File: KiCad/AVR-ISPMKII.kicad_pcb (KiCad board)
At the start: 2 copper layers, 30 x 17.8 mm, 32 parts, among them J1 USB_C_Receptacle_USB2.0, J2 Self_Program, J3 V_Target, J4 ISP_Header, U1 ATmega16U2-MU, U2 AP7365-33WG-7, U3 NLSX4373DMR2G, Y1 16MHz

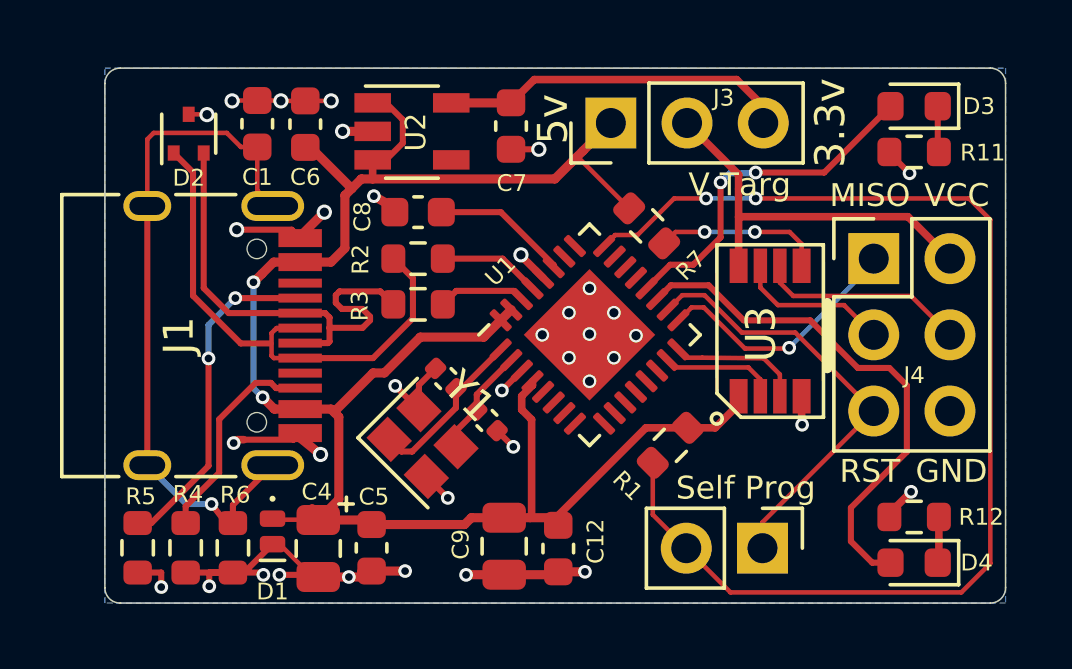
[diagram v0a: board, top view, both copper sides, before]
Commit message: Updated USB trace
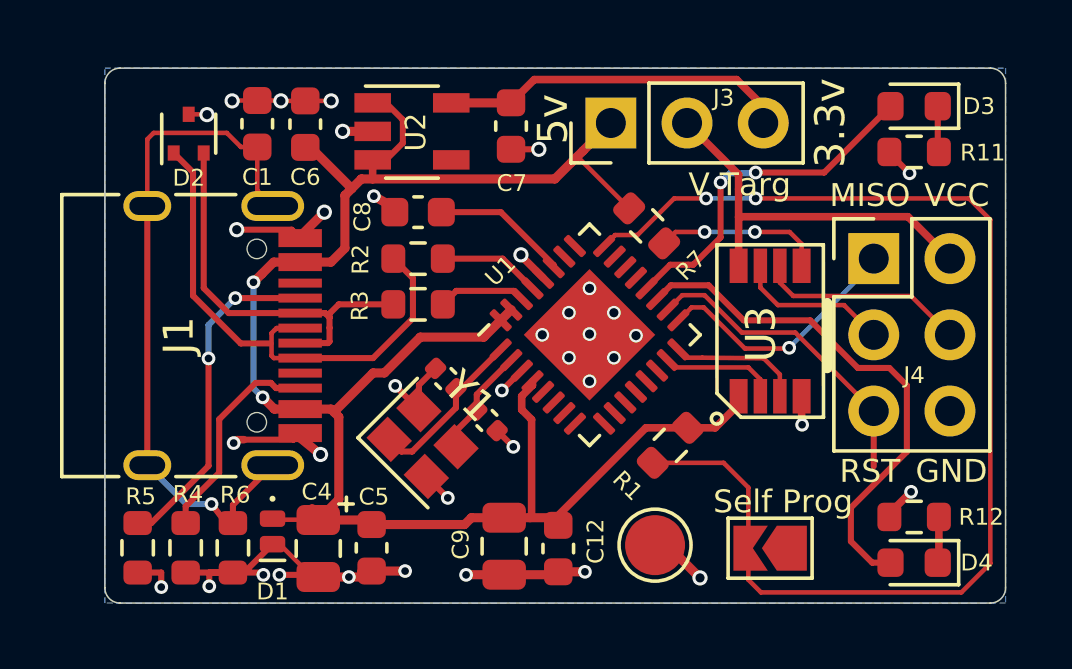
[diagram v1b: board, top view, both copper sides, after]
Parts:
- removed G***: LOGO, logo:mountains
- removed J2: Self_Program, Connector_PinHeader_2.54mm:PinHeader_1x02_P2.54mm_Vertical
- added JP1: SolderJumper_2_Open, Jumper:SolderJumper-2_P1.3mm_Open_TrianglePad1.0x1.5mm, F.Cu at (147.8, 92.2)
- added TP1: TestPoint, TestPoint:TestPoint_Pad_D2.0mm, F.Cu at (144.0, 92.1)
- R11: value 1k -> 22k
- R12: value 1k -> 2.2k
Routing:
- net PB4: track 15.0 -> 10.8 mm
- net /Conn_D-: track 16.3 -> 13.4 mm
- net GND: track 40.4 -> 42.4 mm, vias 36 -> 37
- net RST: track 40.1 -> 41.2 mm
